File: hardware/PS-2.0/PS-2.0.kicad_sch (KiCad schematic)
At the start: 53 parts, among them J1 PinSocket_02x16_P2.54mm_Verti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, J2 Conn_01x05, J3 Conn_01x05, J8 Conn_01x02, J9 Conn_01x02, K1 RAYEX-L90, K2 RAYEX-L90, Q1 IRFPE50, Q2 IRFPE50, Q3 IRFPE50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

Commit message: new file:   hardware/PS-2.0/#auto_saved_files# 	deleted:    hardware/PS-2.0/PS-2.0-backups/PS-2.0-2025-08-01_150036.zip 	deleted:    hardware/PS-2.0/PS-2.0-backups/PS-2.0-2025-08-01_151758.zip 	deleted:    hardware/PS-2.0/PS-2.0-backups/PS-2.0-2025-08-01_152905.zip 	new file:   hardware/PS-2.0/PS-2.0-backups/PS-2.0-2025-08-12_110109.zip 	new file:   hardware/PS-2.0/PS-2.0-backups/PS-2.0-2025-08-12_110823.zip 	new file:   hardware/PS-2.0/PS-2.0-backups/PS-2.0-2025-08-12_111524.zip 	modified:   hardware/PS-2.0/PS-2.0.kicad_sch 	modified:   pic/PS/PS2.0.png
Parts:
- removed H1, H2, H3, H4, H5, H6: MountingHole_Pad, MountingHole:MountingHole_3.2mm_M3_ISO14580_Pad, symbol Mechanical:MountingHole_Pad
- removed HS1, HS2: Heatsink, Heatsink:Heatsink_Stonecold_HS-132_32x14mm_2xFixation1.5mm_NoPad, symbol Mechanical:Heatsink
- removed HS3: Heatsink, Heatsink:Heatsink_Custom_10x18x50, symbol Mechanical:Heatsink
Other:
- moved on the sheet: C1, C2, C3, C4, C5, C6, CON-01, CR1, CR2, D1, D4, D5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

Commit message: deleted:    hardware/PS-2.0/#auto_saved_files# 	deleted:    hardware/PS-2.0/PS-2.0-backups/PS-2.0-2025-08-01_153905.zip 	deleted:    hardware/PS-2.0/PS-2.0-backups/PS-2.0-2025-08-02_150037.zip 	deleted:    hardware/PS-2.0/PS-2.0-backups/PS-2.0-2025-08-05_200710.zip 	renamed:    hardware/PS-2.0/PS-2.0-backups/PS-2.0-2025-08-12_102829.zip -> hardware/PS-2.0/PS-2.0-backups/PS-2.0-2025-08-12_112522.zip 	new file:   hardware/PS-2.0/PS-2.0-backups/PS-2.0-2025-08-12_113033.zip 	new file:   hardware/PS-2.0/PS-2.0-backups/PS-2.0-2025-08-12_113628.zip 	modified:   hardware/PS-2.0/PS-2.0.kicad_pcb 	modified:   hardware/PS-2.0/PS-2.0.kicad_sch 	deleted:    hardware/XF-1.0/XF-1.0-backups/XF-1.0-2025-07-24_194858.zip 	new file:   hardware/XF-1.0/XF-1.0-backups/XF-1.0-2025-08-12_112611.zip 	modified:   pic/PS/PS2.0.png
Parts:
- removed J3: Conn_01x05, Connector_Molex:Molex_KK-396_5273-05A_1x05_P3.96mm_Vertical_2, symbol Connector_Generic:Conn_01x05
- added H1, H2, H3, H4, H5, H6: MountingHole_Pad, MountingHole:MountingHole_3.2mm_M3_ISO14580_Pad, symbol Mechanical:MountingHole_Pad
- added HS1, HS2: Heatsink, Heatsink:Heatsink_Stonecold_HS-132_32x14mm_2xFixation1.5mm_NoPad, symbol Mechanical:Heatsink
- added HS3: Heatsink, Heatsink:Heatsink_Custom_10x18x50, symbol Mechanical:Heatsink
- added J3: Conn_01x05, Connector_Molex:Molex_KK-396_5273-05A_1x05_P3.96mm_Vertical_2, symbol Connector_Generic:Conn_01x03
- J2: symbol Connector_Generic:Conn_01x05 -> Connector_Generic:Conn_01x03
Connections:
- net at J2.2 (Pin_2): now also U2.6 (PAD2)
- net at J2.3 (Pin_3): now also U2.7 (PAD1); no longer U2.6 (PAD2)
- net at U3.5 (CUT): now also J3.1 (Pin_1)
- net at U3.6 (COAG): now also J3.2 (Pin_2)
- net at U3.7 (ACTIVE_M1): now also J3.3 (Pin_3)
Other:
- moved on the sheet: U2, U3

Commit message: modified:   .DS_Store 	modified:   README.md 	deleted:    hardware/PS-2.0/PS-2.0-backups/PS-2.0-2025-08-12_110109.zip 	deleted:    hardware/PS-2.0/PS-2.0-backups/PS-2.0-2025-08-12_110823.zip 	new file:   hardware/PS-2.0/PS-2.0-backups/PS-2.0-2025-08-12_131017.zip 	new file:   hardware/PS-2.0/PS-2.0-backups/PS-2.0-2025-08-12_194453.zip 	modified:   hardware/PS-2.0/PS-2.0.kicad_sch 	deleted:    hardware/PS-2.0/~PS-2.0.kicad_pcb.lck 	deleted:    hardware/PS-2.0/~PS-2.0.kicad_sch.lck 	modified:   hardware/Request PO 20250807 1029.xlsx 	new file:   hardware/XF-1.0/XF-1.0-B_Cu.gbr 	new file:   hardware/XF-1.0/XF-1.0-B_Mask.gbr 	new file:   hardware/XF-1.0/XF-1.0-B_Paste.gbr 	new file:   hardware/XF-1.0/XF-1.0-B_Silkscreen.gbr 	new file:   hardware/XF-1.0/XF-1.0-Edge_Cuts.gbr 	new file:   hardware/XF-1.0/XF-1.0-F_Cu.gbr 	new file:   hardware/XF-1.0/XF-1.0-F_Mask.gbr 	new file:   hardware/XF-1.0/XF-1.0-F_Paste.gbr 	new file:   hardware/XF-1.0/XF-1.0-F_Silkscreen.gbr 	new file:   hardware/XF-1.0/XF-1.0-NPTH.drl 	new file:   hardware/XF-1.0/XF-1.0-PTH.drl 	deleted:    hardware/XF-1.0/XF-1.0-backups/XF-1.0-2025-07-24_195648.zip 	deleted:    hardware/XF-1.0/XF-1.0-backups/XF-1.0-2025-07-24_200323.zip 	deleted:    hardware/XF-1.0/XF-1.0-backups/XF-1.0-2025-07-24_200926.zip 	new file:   hardware/XF-1.0/XF-1.0-backups/XF-1.0-2025-08-12_131501.zip 	new file:   hardware/XF-1.0/XF-1.0-backups/XF-1.0-2025-08-12_133029.zip 	new file:   hardware/XF-1.0/XF-1.0-backups/XF-1.0-2025-08-12_151757.zip 	new file:   hardware/XF-1.0/XF-1.0-job.gbrjob 	modified:   hardware/XF-1.0/XF-1.0.kicad_pcb 	modified:   pic/.DS_Store 	new file:   pic/PS/400kHz/1/400kHz-1-comparison.png 	deleted:    pic/PS/400kHz/1/LC-29u-3n3/PS2.0.png 	new file:   pic/PS/400kHz/1/LC-29u-3n3/comparison.drawio 	new file:   pic/PS/400kHz/3/LC-47u-3n3/comparison.drawio 	modified:   pic/Reverse Engineering/.DS_Store 	new file:   pic/Reverse Engineering/20kHz/RigolDS0.png 	new file:   pic/Reverse Engineering/20kHz/RigolDS1.png 	n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
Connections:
- net PWM-EN: no longer C1.1, U1.1 (VDD), U1.8 (VDD)
- net OUT-: now reaches C5.1, C6.1, CR2.2, D4.2 (A), K2.11A, K2.11B
- net OUT+: now reaches C4.1, C5.2, C6.2, K1.11A, K1.11B, L7.2
- new net +12V: C1.1, U1.1 (VDD), U1.8 (VDD)
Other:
- moved on the sheet: C1, C2, C3, C4, C5, C6, CON-01, CR1, CR2, D1, D2, D3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

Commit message: modified:   README.md 	deleted:    hardware/PS-2.0/PS-2.0-backups/PS-2.0-2025-08-12_111524.zip 	new file:   hardware/PS-2.0/PS-2.0-backups/PS-2.0-2025-08-13_131332.zip 	modified:   hardware/PS-2.0/PS-2.0.kicad_sch
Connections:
- net +12V is gone; now on net PWM-EN: C1.1, U1.1 (VDD), U1.8 (VDD)
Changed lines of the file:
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@@
 	)
 	(junction
+		(at 78.74 68.58)
+		(diameter 0)
+		(color 0 0 0 0)
+	)
+	(junction
 		(at 36.83 95.25)
 		(diameter 0)
@@
 	)
 	(junction
-		(at 78.74 68.58)
-		(diameter 0)
-		(color 0 0 0 0)
-	)
-	(junction
 		(at 74.93 161.29)
 		(diameter 0)
@@
 	(wire
 		(pts
+			(xy 73.66 40.64) (xy 73.66 82.55)
+		)
+		(stroke
+			(width 0)
+			(type default)
+		)
+	)
+	(wire
+		(pts
 			(xy 229.87 161.29) (xy 229.87 134.62)
 		)
@@
 	(wire
 		(pts
+			(xy 78.74 43.18) (xy 78.74 68.58)
+		)
+		(stroke
+			(width 0)
+			(type default)
+		)
+	)
+	(wire
+		(pts
 			(xy 196.85 83.82) (xy 201.93 83.82)
 		)
@@
 	(wire
 		(pts
-			(xy 78.74 66.04) (xy 78.74 68.58)
-		)
-		(stroke
-			(width 0)
-			(type default)
-		)
-	)
-	(wire
-		(pts
 			(xy 113.03 86.36) (xy 113.03 82.55)
 		)
@@
 	(wire
 		(pts
-			(xy 62.23 82.55) (xy 83.82 82.55)
+			(xy 73.66 82.55) (xy 83.82 82.55)
 		)
 		(stroke
@@
 		)
 	)
-	(label "PWM"
-		(at 62.23 82.55 0)
-		(fields_autoplaced yes)
-		(effects
-			(font
-				(size 1.27 1.27)
-			)
-			(justify left bottom)
-		)
-	)
 	(label "PWM-EN"
 		(at 24.13 43.18 0)
@@
 					(unit 1)
 				)
-			)
-		)
-	)
-	(symbol
-		(lib_id "power:+12V")
-		(at 78.74 66.04 0)
-		(unit 1)
-		(exclude_from_sim no)
-		(in_bom yes)
-		(on_board yes)
-		(dnp no)
-		(fields_autoplaced yes)
-		(property "Reference" "#PWR09"
-			(at 78.74 69.85 0)
-			(effects
-				(font
-					(size 1.27 1.27)
-				)
-				(hide yes)
-			)
-		)
-		(property "Value" "+12V"
-			(at 78.74 60.96 0)
-			(effects
-				(font
-					(size 1.27 1.27)
-				)
-			)
-		)
-		(property "Footprint" ""
-			(at 78.74 66.04 0)
-			(effects
-				(font
-					(size 1.27 1.27)
-				)
-				(hide yes)
-			)
-		)
-		(property "Datasheet" ""
-			(at 78.74 66.04 0)
-			(effects
-				(font
-					(size 1.27 1.27)
-				)
-				(hide yes)
-			)
-		)
-		(property "Description" "Power symbol creates a global label with name \"+12V\""
-			(at 78.74 66.04 0)
-			(effects
-				(font
-					(size 1.27 1.27)
-				)
-				(hide yes)
-			)
-		)
-		(pin "1"
-		)
-		(instances
-			(project ""
-				(path "/3a4da535-700d-4512-9d93-355e5c375ab5"
-					(reference "#PWR09")
-					(unit 1)
-				)

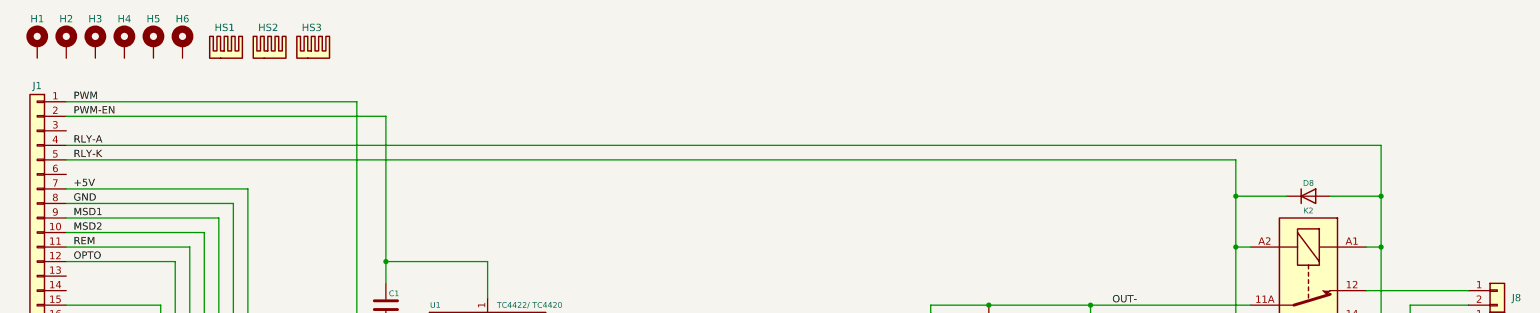
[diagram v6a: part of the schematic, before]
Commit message: modified:   .DS_Store 	modified:   Ferrite Transformer Calculation.xlsx 	modified:   README.md 	modified:   firmware/ESP32-S3 PWM/src/main.cpp 	deleted:    hardware/CTL-3.0/.~BoM.xlsx 	new file:   hardware/CTL-3.0/CTL-3.0-backups/CTL-3.0-2025-08-19_103125.zip 	new file:   hardware/CTL-4.0/BoM.xlsx 	new file:   hardware/CTL-4.0/CTL-4.0-backups/CTL-4.0-2025-08-19_120538.zip 	new file:   hardware/CTL-4.0/CTL-4.0-backups/CTL-4.0-2025-08-19_134756.zip 	new file:   hardware/CTL-4.0/CTL-4.0-backups/CTL-4.0-2025-08-19_140213.zip 	new file:   hardware/CTL-4.0/CTL-4.0-backups/CTL-4.0-2025-08-19_140737.zip 	new file:   hardware/CTL-4.0/CTL-4.0-backups/CTL-4.0-2025-08-19_153532.zip 	new file:   hardware/CTL-4.0/CTL-4.0-backups/CTL-4.0-2025-08-20_101945.zip 	new file:   hardware/CTL-4.0/CTL-4.0-backups/CTL-4.0-2025-08-22_150818.zip 	new file:   hardware/CTL-4.0/CTL-4.0.FCStd 	new file:   hardware/CTL-4.0/CTL-4.0.iges 	new file:   hardware/CTL-4.0/CTL-4.0.kicad_pcb 	new file:   hardware/CTL-4.0/CTL-4.0.kicad_prl 	new file:   hardware/CTL-4.0/CTL-4.0.kicad_pro 	new file:   hardware/CTL-4.0/CTL-4.0.kicad_sch 	new file:   hardware/CTL-4.0/CTL-4.0.png 	new file:   hardware/CTL-4.0/CTL-4.0.step 	new file:   hardware/CTL-4.0/fp-info-cache 	new file:   hardware/CTL-4.0/~CTL-4.0.kicad_sch.lck 	deleted:    hardware/PS-2.0/PS-2.0-backups/PS-2.0-2025-08-05_201831.zip 	deleted:    hardware/PS-2.0/PS-2.0-backups/PS-2.0-2025-08-05_205329.zip 	deleted:    hardware/PS-2.0/PS-2.0-backups/PS-2.0-2025-08-05_210221.zip 	deleted:    hardware/PS-2.0/PS-2.0-backups/PS-2.0-2025-08-05_211355.zip 	deleted:    hardware/PS-2.0/PS-2.0-backups/PS-2.0-2025-08-06_131643.zip 	deleted:    hardware/PS-2.0/PS-2.0-backups/PS-2.0-2025-08-06_132702.zip 	deleted:    hardware/PS-2.0/PS-2.0-backups/PS-2.0-2025-08-06_133543.zip 	new file:   hardware/PS-2.0/PS-2.0-backups/PS-2.0-2025-08-19_135413.zip 	new file:   hardware/PS-2.0/PS-2.0-backups/PS-2.0-2025-08-19_135951.zip 	new file:   hardware/PS-2.0/PS-2.0-backups/PS-2.0-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
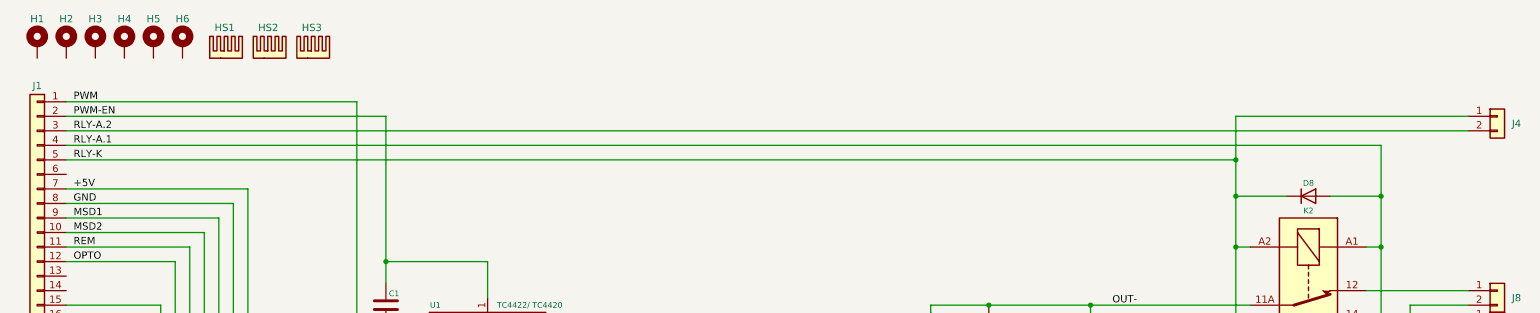
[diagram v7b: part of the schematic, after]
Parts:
- added J4: Conn_01x02, Connector_Molex:Molex_KK-396_5273-02A_1x02_P3.96mm_Vertical, symbol Connector_Generic:Conn_01x02
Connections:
- net RLY-K: now also J4.1 (Pin_1)
- net RLY-A.2: now reaches J1.3 (Pin_3)
- net RLY-A.2: now also J4.2 (Pin_2)
- net RLY-A renamed RLY-A.1
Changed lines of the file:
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@@
 	)
 	(junction
+		(at 227.33 50.8)
+		(diameter 0)
+		(color 0 0 0 0)
+	)
+	(junction
 		(at 252.73 115.57)
 		(diameter 0)
@@
 	(wire
 		(pts
+			(xy 227.33 43.18) (xy 227.33 50.8)
+		)
+		(stroke
+			(width 0)
+			(type default)
+		)
+	)
+	(wire
+		(pts
 			(xy 250.19 124.46) (xy 252.73 124.46)
 		)
@@
 	(wire
 		(pts
+			(xy 22.86 45.72) (xy 267.97 45.72)
+		)
+		(stroke
+			(width 0)
+			(type default)
+		)
+	)
+	(wire
+		(pts
 			(xy 41.91 68.58) (xy 41.91 130.81)
 		)
@@
 	(wire
 		(pts
+			(xy 267.97 43.18) (xy 227.33 43.18)
+		)
+		(stroke
+			(width 0)
+			(type default)
+		)
+	)
+	(wire
+		(pts
 			(xy 252.73 66.04) (xy 252.73 115.57)
 		)
@@
 		)
 	)
+	(label "RLY-A.2"
+		(at 24.13 45.72 0)
+		(fields_autoplaced yes)
+		(effects
+			(font
+				(size 1.27 1.27)
+			)
+			(justify left bottom)
+		)
+	)
 	(label "PWM-EN"
 		(at 24.13 43.18 0)
@@
 		)
 	)
-	(label "RLY-A"
+	(label "RLY-A.1"
 		(at 24.13 48.26 0)
 		(fields_autoplaced yes)
@@
 					(unit 1)
 				)
+			)
+		)
+	)
+	(symbol
+		(lib_id "Connector_Generic:Conn_01x02")
+		(at 273.05 43.18 0)
+		(unit 1)
+		(exclude_from_sim no)
+		(in_bom yes)
+		(on_board yes)
+		(dnp no)
+		(fields_autoplaced yes)
+		(property "Reference" "J4"
+			(at 275.59 44.4499 0)
+			(effects
+				(font
+					(size 1.27 1.27)
+				)
+				(justify left)
+			)
+		)
+		(property "Value" "Conn_01x02"
+			(at 275.59 45.7199 0)
+			(effects
+				(font
+					(size 1.27 1.27)
+				)
+				(justify left)
+				(hide yes)
+			)
+		)
+		(property "Footprint" "Connector_Molex:Molex_KK-396_5273-02A_1x02_P3.96mm_Vertical"
+			(at 273.05 43.18 0)
+			(effects
+				(font
+					(size 1.27 1.27)
+				)
+				(hide yes)
+			)
+		)
+		(property "Datasheet" "~"
+			(at 273.05 43.18 0)
+			(effects
+				(font
+					(size 1.27 1.27)
+				)
+				(hide yes)
+			)
+		)
+		(property "Description" "Generic connector, single row, 01x02, script generated (kicad-library-utils/schlib/autogen/connector/)"
+			(at 273.05 43.18 0)
+			(effects
+				(font
+					(size 1.27 1.27)
+				)
+				(hide yes)
+			)
+		)
+		(pin "2"
+		)
+		(pin "1"
+		)
+		(instances
+			(project "PS-2.0"
+				(path "/3a4da535-700d-4512-9d93-355e5c375ab5"
+					(reference "J4")
+					(unit 1)
+				)
